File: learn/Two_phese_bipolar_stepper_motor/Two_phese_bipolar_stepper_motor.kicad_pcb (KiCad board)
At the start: 2 copper layers, 73.7 x 81 mm, 25 parts, among them J1 Screw_Terminal_01x02, J2 Screw_Terminal_01x02, J3 Screw_Terminal_01x12, J4 Screw_Terminal_01x04, U1 L297, U2 L298N

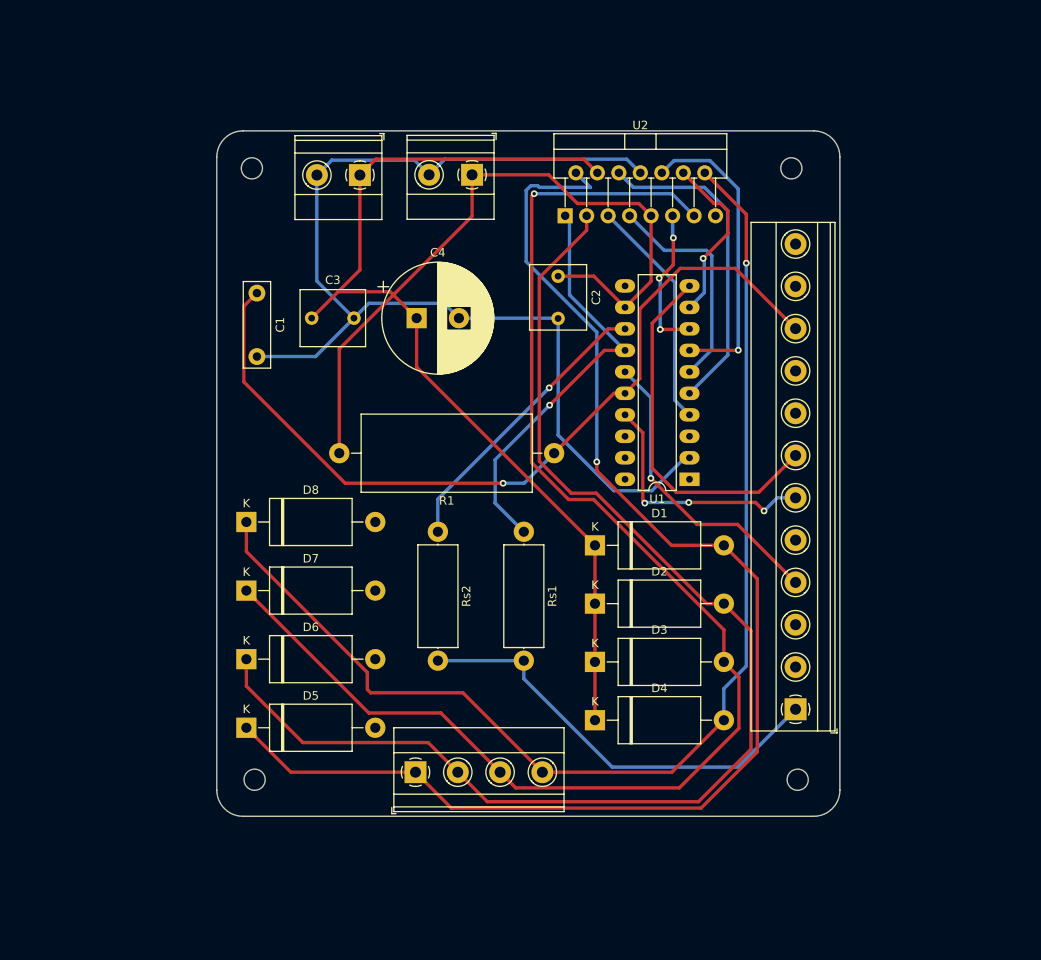
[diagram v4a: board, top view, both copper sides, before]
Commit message: two_phase: clean the wrong wire and to do the new wire. Now the pcb is finisc
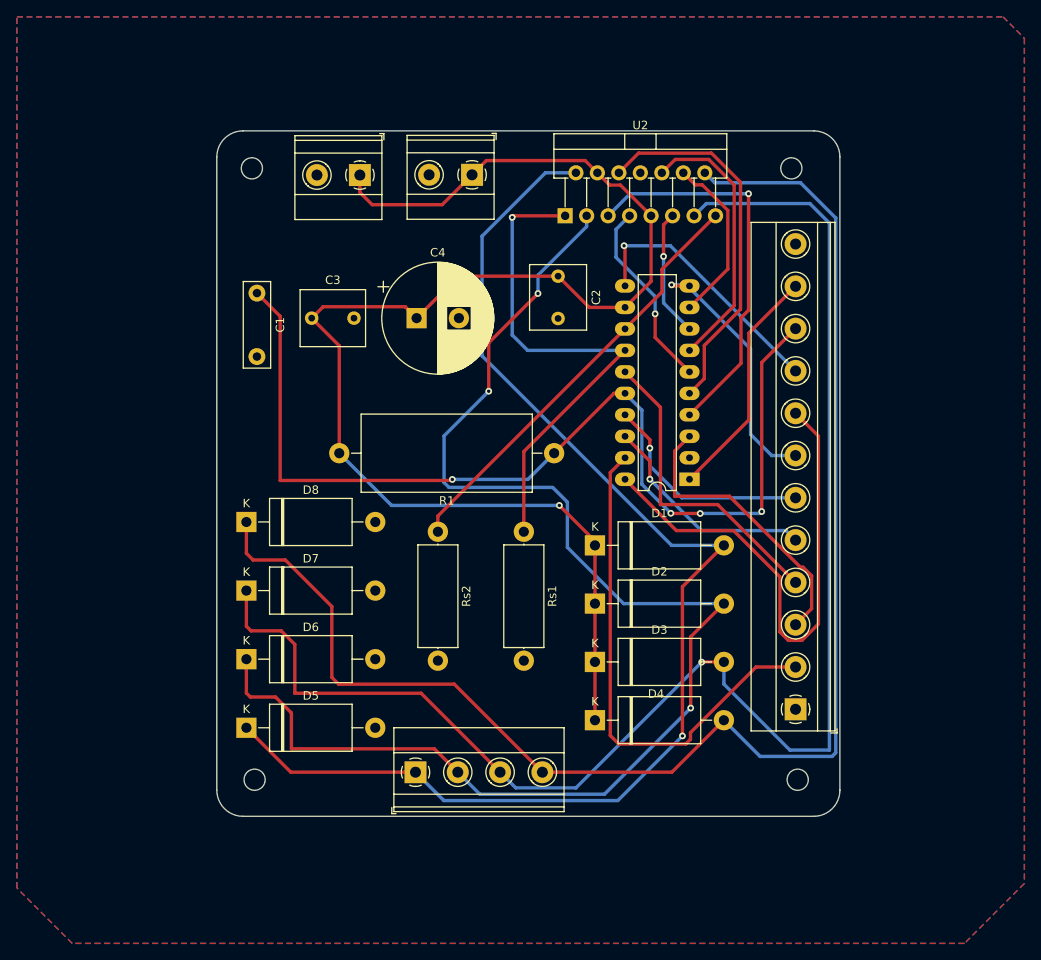
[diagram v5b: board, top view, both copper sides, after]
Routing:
- net GND: track 184.6 -> 1.17 mm
- net /RESET: track 0.00 -> 61.4 mm
- net /HALF: track 0.00 -> 60.1 mm
- net /HOME: track 0.00 -> 34.5 mm
- net Net-(D4-A): track 142.3 -> 174.4 mm, vias 1 -> 0
- net /CTRL: track 0.00 -> 31.2 mm, vias 0 -> 1
- net VS: track 199.8 -> 168.8 mm, vias 0 -> 1
- net /SYNC: track 0.00 -> 28.0 mm
- net /CLK: track 0.00 -> 26.5 mm, vias 0 -> 1
- net /OSC: track 99.6 -> 118.9 mm, vias 1 -> 4
- net Net-(U1-A): track 27.5 -> 46.7 mm, vias 0 -> 1
- net /Rs2: track 34.3 -> 50.9 mm, vias 1 -> 0
- net Net-(D2-A): track 149.7 -> 162.8 mm, vias 0 -> 3
- net /ENA: track 43.3 -> 31.1 mm, vias 0 -> 1
- net /Rs1: track 49.5 -> 61.5 mm
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- added copper zone on B.Cu, net GND
- added copper zone on F.Cu, net GND

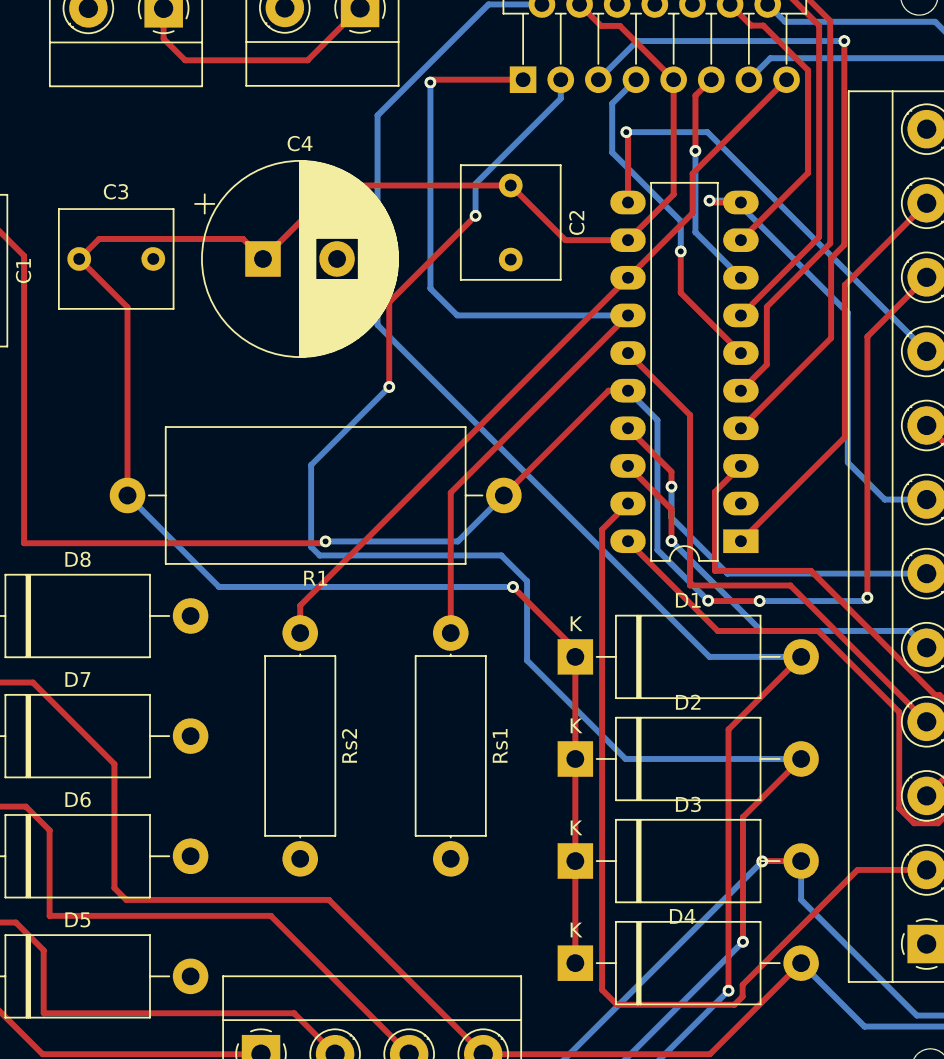
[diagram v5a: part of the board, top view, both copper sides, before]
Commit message: two_phase: labeling the connectors
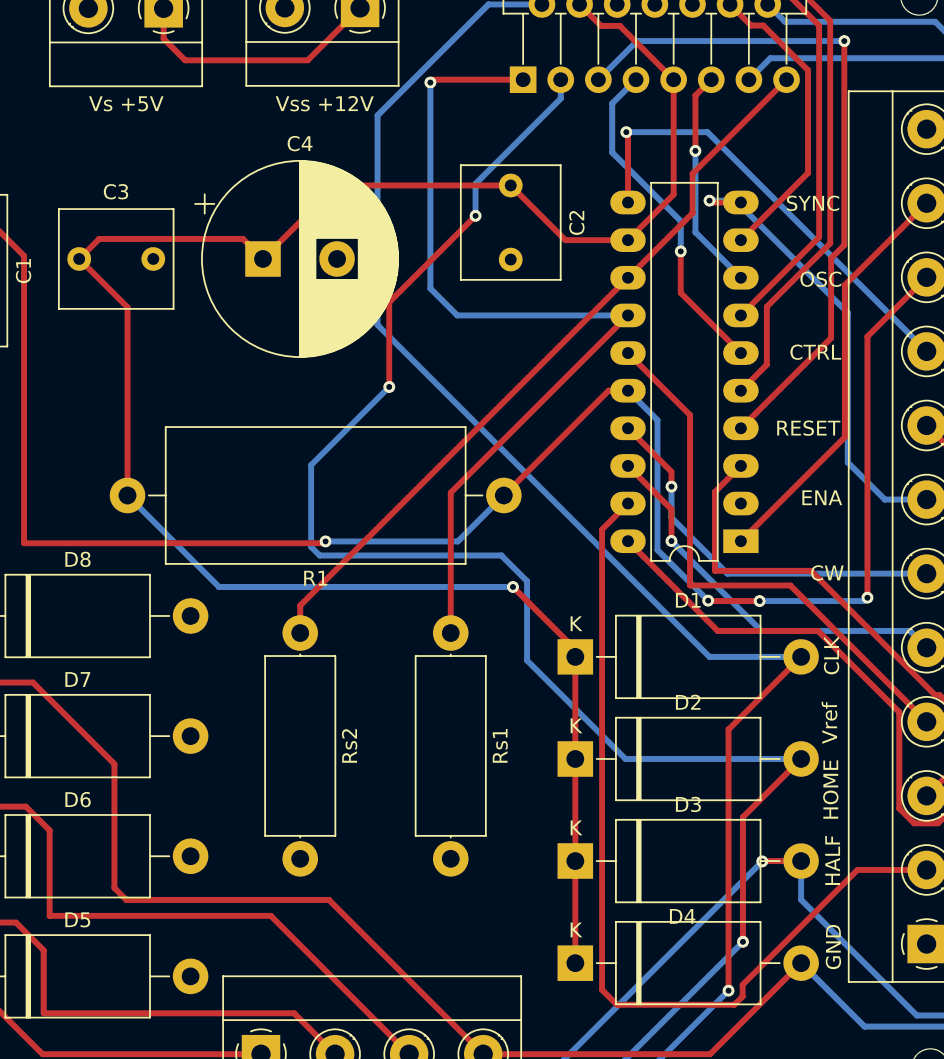
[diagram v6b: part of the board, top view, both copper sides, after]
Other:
- board text added: "CLK"
- board text added: "CTRL"
- board text added: "CW"
- board text added: "ENA"
- board text added: "GND"
- board text added: "HALF"
- board text added: "HOME"
- board text added: "OSC"
- board text added: "RESET"
- board text added: "SYNC"
- board text added: "Vref"
- board text added: "Vs +5V"
- board text added: "Vss +12V"
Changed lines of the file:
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@@
   (gr_line (start 113.029957 55.410043) (end 113.029957 130.26)
     (stroke (width 0.1) (type default)) (layer "Edge.Cuts"))
+  (gr_text "HOME" (at 175.6 112.375 90) (layer "F.SilkS")
+    (effects (font (size 1 1) (thickness 0.15)) (justify left bottom))
+  )
+  (gr_text "SYNC" (at 171.925 71.325) (layer "F.SilkS")
+    (effects (font (size 1 1) (thickness 0.15)) (justify left bottom))
+  )
+  (gr_text "Vs +5V" (at 124.9 64.6) (layer "F.SilkS")
+    (effects (font (size 1 1) (thickness 0.15)) (justify left bottom))
+  )
+  (gr_text "CW" (at 173.575 96.275) (layer "F.SilkS")
+    (effects (font (size 1 1) (thickness 0.15)) (justify left bottom))
+  )
+  (gr_text "Vss +12V" (at 137.5 64.6) (layer "F.SilkS")
+    (effects (font (size 1 1) (thickness 0.15)) (justify left bottom))
+  )
+  (gr_text "CLK" (at 175.65 102.575 90) (layer "F.SilkS")
+    (effects (font (size 1 1) (thickness 0.15)) (justify left bottom))
+  )
+  (gr_text "ENA" (at 172.925 91.2) (layer "F.SilkS")
+    (effects (font (size 1 1) (thickness 0.15)) (justify left bottom))
+  )
+  (gr_text "Vref" (at 175.525 107.2 90) (layer "F.SilkS")
+    (effects (font (size 1 1) (thickness 0.15)) (justify left bottom))
+  )
+  (gr_text "CTRL" (at 172.175 81.375) (layer "F.SilkS")
+    (effects (font (size 1 1) (thickness 0.15)) (justify left bottom))
+  )
+  (gr_text "RESET" (at 171.225 86.5) (layer "F.SilkS")
+    (effects (font (size 1 1) (thickness 0.15)) (justify left bottom))
+  )
+  (gr_text "HALF" (at 175.725 116.85 90) (layer "F.SilkS")
+    (effects (font (size 1 1) (thickness 0.15)) (justify left bottom))
+  )
+  (gr_text "OSC" (at 172.85 76.45) (layer "F.SilkS")
+    (effects (font (size 1 1) (thickness 0.15)) (justify left bottom))
+  )
+  (gr_text "GND" (at 175.775 122.475 90) (layer "F.SilkS")
+    (effects (font (size 1 1) (thickness 0.15)) (justify left bottom))
+  )
   (segment (start 159.982 83.35) (end 161.29 83.35) (width 0.4) (layer "F.Cu") (net 1))
   (segment (start 120.525 93.65) (end 140.75 93.65) (width 0.4) (layer "F.Cu") (net 1))

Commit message: two_phase: new lablel out 1 out2 out3 out4
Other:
- board text added: "OUT1"
- board text added: "OUT2"
- board text added: "OUT3"
- board text added: "OUT4"
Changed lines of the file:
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@@
     (property "ki_keywords" "diode Schottky")
     (attr through_hole)
-    (fp_text reference "D4" (at 7.216 -3.115) (layer "F.SilkS")
+    (fp_text reference "D4" (at 7.541 -3.415) (layer "F.SilkS")
         (effects (font (size 1 1) (thickness 0.15)))
     )
@@
     (effects (font (size 1 1) (thickness 0.15)) (justify left bottom))
   )
+  (gr_text "OUT2" (at 141.625 121.275) (layer "F.SilkS")
+    (effects (font (size 1 1) (thickness 0.15)))
+  )
+  (gr_text "OUT1" (at 136.725 121.275) (layer "F.SilkS")
+    (effects (font (size 1 1) (thickness 0.15)))
+  )
   (gr_text "ENA" (at 172.925 91.2) (layer "F.SilkS")
     (effects (font (size 1 1) (thickness 0.15)) (justify left bottom))
@@
     (effects (font (size 1 1) (thickness 0.15)) (justify left bottom))
   )
+  (gr_text "OUT4" (at 151.425 121.275) (layer "F.SilkS")
+    (effects (font (size 1 1) (thickness 0.15)))
+  )
   (gr_text "CTRL" (at 172.175 81.375) (layer "F.SilkS")
     (effects (font (size 1 1) (thickness 0.15)) (justify left bottom))
   )
+  (gr_text "OUT3" (at 146.525 121.275) (layer "F.SilkS")
+    (effects (font (size 1 1) (thickness 0.15)))
+  )
   (gr_text "RESET" (at 171.225 86.5) (layer "F.SilkS")
